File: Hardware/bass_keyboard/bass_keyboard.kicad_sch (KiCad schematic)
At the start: 188 parts, among them J1 Conn_02x17_Top_Bottom

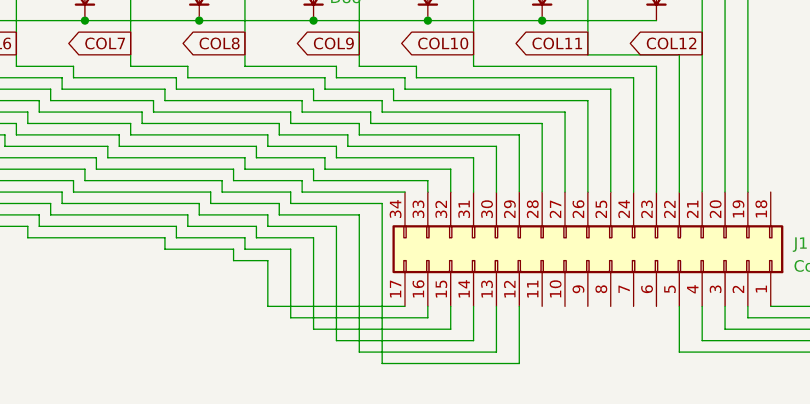
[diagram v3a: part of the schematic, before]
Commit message: Redo traces on bass keyboard
Completely started over on the traces, decided that the automatic routing was whack. Much happier with the new layout, increased orderliness and legibility, less prone to manufacturing error due to via clearance. Also adjusted speaker connection to better fit 16 AWG speaker wire.
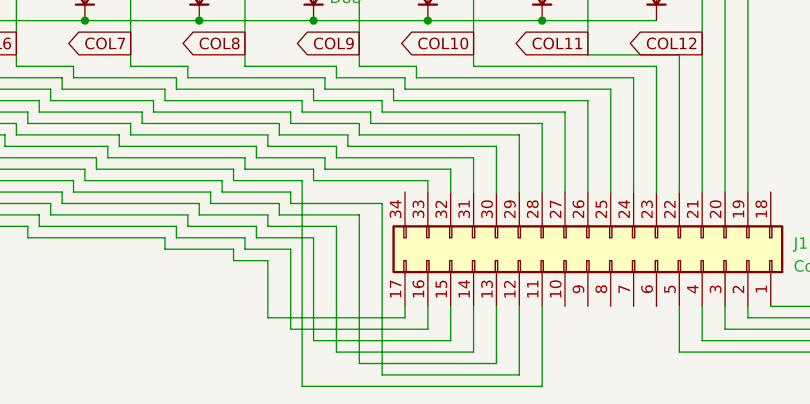
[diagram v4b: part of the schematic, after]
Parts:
- LS1: footprint Connector_Wire:SolderWire-2sqmm_1x02_P7.8mm_D2mm_OD3.9mm -> Connector_Wire:SolderWire-1sqmm_1x02_P5.4mm_D1.4mm_OD2.7mm
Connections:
- net ROW6: now also J1.11 (Pin_11); no longer J1.34 (Pin_34)
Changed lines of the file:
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@@
     (stroke (width 0) (type default))
   )
+  (wire (pts (xy 191.77 157.48) (xy 191.77 156.21))
+    (stroke (width 0) (type default))
+  )
   (wire (pts (xy 128.27 69.85) (xy 133.35 69.85))
     (stroke (width 0) (type default))
@@
     (stroke (width 0) (type default))
   )
-  (wire (pts (xy 180.34 143.51) (xy 191.77 143.51))
-    (stroke (width 0) (type default))
-  )
   (wire (pts (xy 97.79 57.15) (xy 102.87 57.15))
     (stroke (width 0) (type default))
@@
     (stroke (width 0) (type default))
   )
-  (wire (pts (xy 201.93 161.29) (xy 186.69 161.29))
+  (wire (pts (xy 201.93 162.56) (xy 186.69 162.56))
     (stroke (width 0) (type default))
   )
@@
     (stroke (width 0) (type default))
   )
+  (wire (pts (xy 180.34 165.1) (xy 207.01 165.1))
+    (stroke (width 0) (type default))
+  )
   (wire (pts (xy 176.53 82.55) (xy 176.53 88.9))
     (stroke (width 0) (type default))
@@
     (stroke (width 0) (type default))
   )
-  (wire (pts (xy 196.85 156.21) (xy 196.85 158.75))
+  (wire (pts (xy 196.85 156.21) (xy 196.85 160.02))
     (stroke (width 0) (type default))
   )
@@
     (stroke (width 0) (type default))
   )
-  (wire (pts (xy 194.31 157.48) (xy 179.07 157.48))
+  (wire (pts (xy 194.31 158.75) (xy 179.07 158.75))
     (stroke (width 0) (type default))
   )
@@
     (stroke (width 0) (type default))
   )
-  (wire (pts (xy 180.34 142.24) (xy 180.34 143.51))
+  (wire (pts (xy 180.34 142.24) (xy 180.34 165.1))
     (stroke (width 0) (type default))
   )
@@
     (stroke (width 0) (type default))
   )
-  (wire (pts (xy 176.53 151.13) (xy 176.53 156.21))
+  (wire (pts (xy 176.53 151.13) (xy 176.53 157.48))
     (stroke (width 0) (type default))
   )
@@
     (stroke (width 0) (type default))
   )
-  (wire (pts (xy 191.77 156.21) (xy 176.53 156.21))
+  (wire (pts (xy 191.77 157.48) (xy 176.53 157.48))
     (stroke (width 0) (type default))
   )
@@
     (stroke (width 0) (type default))
   )
-  (wire (pts (xy 199.39 156.21) (xy 199.39 160.02))
+  (wire (pts (xy 199.39 156.21) (xy 199.39 161.29))
     (stroke (width 0) (type default))
   )
@@
     (stroke (width 0) (type default))
   )
-  (wire (pts (xy 201.93 156.21) (xy 201.93 161.29))
+  (wire (pts (xy 201.93 156.21) (xy 201.93 162.56))
     (stroke (width 0) (type default))
   )
@@
     (stroke (width 0) (type default))
   )
+  (wire (pts (xy 207.01 165.1) (xy 207.01 156.21))
+    (stroke (width 0) (type default))
+  )
   (wire (pts (xy 148.59 50.8) (xy 148.59 57.15))
     (stroke (width 0) (type default))
@@
     (stroke (width 0) (type default))
   )
-  (wire (pts (xy 186.69 146.05) (xy 186.69 161.29))
+  (wire (pts (xy 186.69 146.05) (xy 186.69 162.56))
     (stroke (width 0) (type default))
   )
@@
     (stroke (width 0) (type default))
   )
-  (wire (pts (xy 181.61 148.59) (xy 181.61 158.75))
+  (wire (pts (xy 181.61 148.59) (xy 181.61 160.02))
     (stroke (width 0) (type default))
   )
@@
     (stroke (width 0) (type default))
   )
-  (wire (pts (xy 204.47 162.56) (xy 189.23 162.56))
+  (wire (pts (xy 204.47 163.83) (xy 189.23 163.83))
     (stroke (width 0) (type default))
   )
@@
     (stroke (width 0) (type default))
   )
-  (wire (pts (xy 179.07 149.86) (xy 179.07 157.48))
+  (wire (pts (xy 179.07 149.86) (xy 179.07 158.75))
     (stroke (width 0) (type default))
   )
@@
     (stroke (width 0) (type default))
   )
-  (wire (pts (xy 196.85 158.75) (xy 181.61 158.75))
+  (wire (pts (xy 196.85 160.02) (xy 181.61 160.02))
     (stroke (width 0) (type default))
   )
@@
     (stroke (width 0) (type default))
   )
-  (wire (pts (xy 199.39 160.02) (xy 184.15 160.02))
+  (wire (pts (xy 199.39 161.29) (xy 184.15 161.29))
     (stroke (width 0) (type default))
   )
@@
     (stroke (width 0) (type default))
   )
-  (wire (pts (xy 204.47 156.21) (xy 204.47 162.56))
+  (wire (pts (xy 204.47 156.21) (xy 204.47 163.83))
     (stroke (width 0) (type default))
   )
@@
     (stroke (width 0) (type default))
   )
-  (wire (pts (xy 184.15 147.32) (xy 184.15 160.02))
+  (wire (pts (xy 184.15 147.32) (xy 184.15 161.29))
     (stroke (width 0) (type default))
   )
@@
     (stroke (width 0) (type default))
   )
-  (wire (pts (xy 194.31 156.21) (xy 194.31 157.48))
+  (wire (pts (xy 194.31 156.21) (xy 194.31 158.75))
     (stroke (width 0) (type default))
   )
@@
     (stroke (width 0) (type default))
   )
-  (wire (pts (xy 189.23 144.78) (xy 189.23 162.56))
+  (wire (pts (xy 189.23 144.78) (xy 189.23 163.83))
     (stroke (width 0) (type default))
   )
@@
       (effects (font (size 1.27 1.27)) (justify left))
     )
-    (property "Footprint" "Connector_Wire:SolderWire-2sqmm_1x02_P7.8mm_D2mm_OD3.9mm" (at 234.95 53.34 0)
+    (property "Footprint" "Connector_Wire:SolderWire-1sqmm_1x02_P5.4mm_D1.4mm_OD2.7mm" (at 234.95 53.34 0)
       (effects (font (size 1.27 1.27)) hide)
     )
